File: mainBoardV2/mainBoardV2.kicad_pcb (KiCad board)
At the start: 2 copper layers, 42.8 x 40.5 mm, 30 parts, among them J1 USB4125-GF-A_REVA2, U3 MCP73871-2AAI_ML, U4 MPU6050_Module, U5 TPS61023DRLT

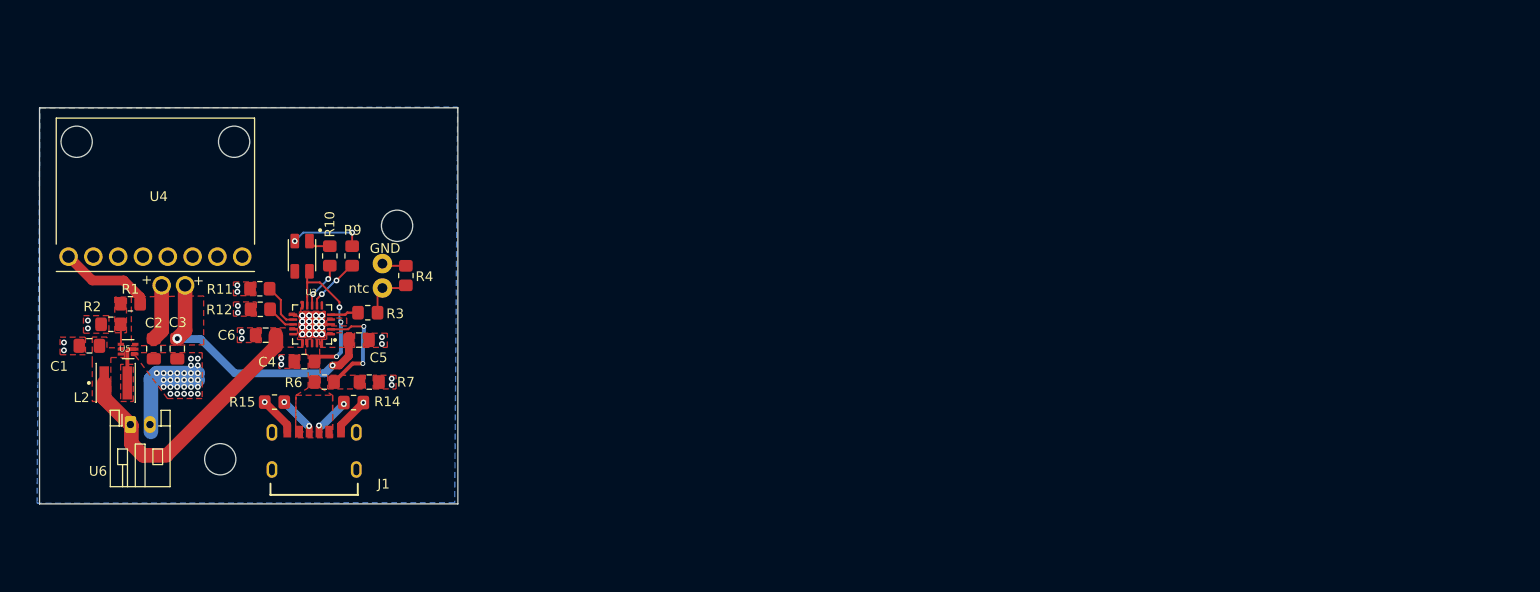
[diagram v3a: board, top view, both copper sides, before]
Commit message: 3.17.26.C2
Added tantalum capacitors to output of boost converter. Have created gerber and drill files after running DRC check until only thing left were some clearance warnings. manufacturer can handle.
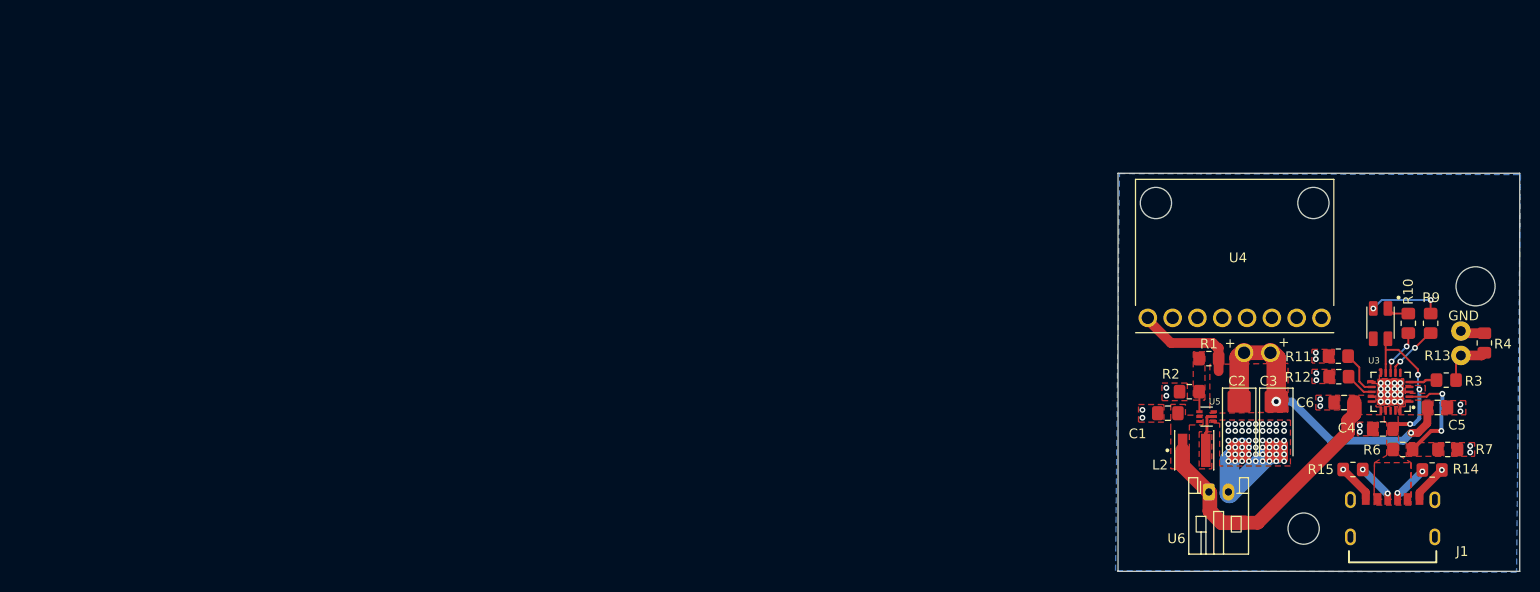
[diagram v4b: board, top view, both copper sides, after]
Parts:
- C2, C3: footprint Capacitor_SMD:C_0805_2012Metric_Pad1.18x1.45mm_HandSolder -> Capacitor_Tantalum_SMD:CP_EIA-6032-15_Kemet-U_HandSolder
- R10: value 470k -> 300
- R9: value 470k -> 160
- moved C3 112.8 mm to (216.8, 125.3)
- moved C2 111.4 mm to (213.0, 125.3)
- moved ? 111.3 mm to (216.2, 117.7)
- moved ? 111.1 mm to (219.6, 135.7)
- moved ? 111.0 mm to (213.5, 117.7)
- moved U4 110.7 mm to (212.5, 107.8)
- moved C5 110.6 mm to (233.3, 123.3)
- moved C6 110.6 mm to (223.8, 122.8)
- moved J1 110.6 mm to (228.7, 135.8)
- moved L2 110.6 mm to (208.4, 127.7)
- moved R10 110.6 mm to (230.3, 114.7)
- moved R11 110.6 mm to (223.2, 118.0)
- moved R14 110.6 mm to (232.8, 129.7)
- moved R15 110.6 mm to (224.7, 129.7)
- moved R2 110.6 mm to (207.9, 121.7)
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- renumbered ntc to R13
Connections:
- U4 pad GND: unconnected-(U4-PadGND) -> GND
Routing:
- net GND: track 26.4 -> 22.8 mm, vias 78 -> 88
- net /VBatt+: track 28.4 -> 30.3 mm
- net /VoutBoost: track 42.7 -> 43.6 mm
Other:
- board size 42.8 x 40.5 mm -> 41.1 x 40.7 mm

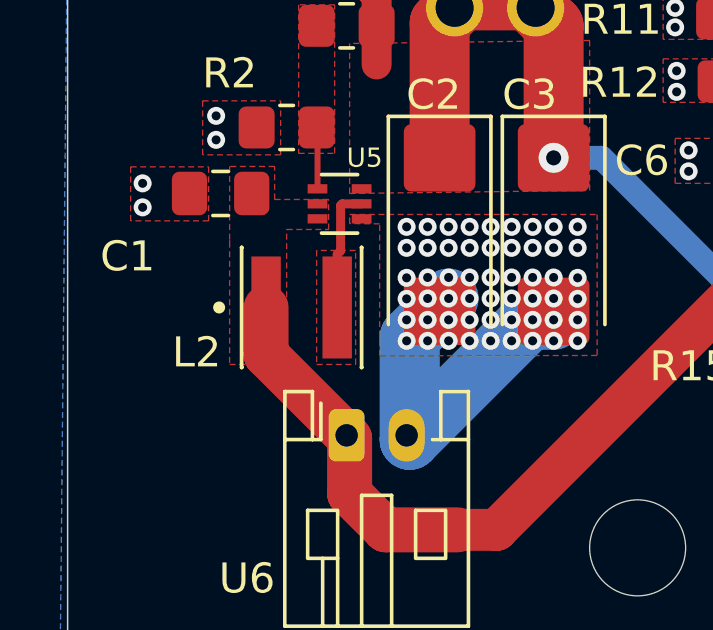
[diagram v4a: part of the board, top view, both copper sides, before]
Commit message: 3.22.26.C1
Added replacement inductor footprint and symbol to library. Updated board and schematic files with new component, but now gerber job files are not coming out correctly. Look transparent in a Gerber Viewer.
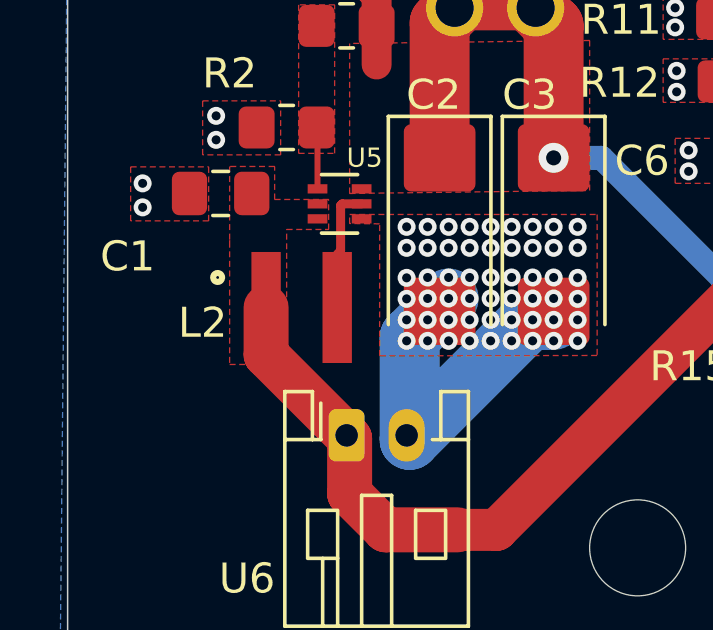
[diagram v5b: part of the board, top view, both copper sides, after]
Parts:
- L2: footprint XEL4030-102MEC:IND_XEL4030-102MEC -> WE-MAPI_4030:WE-MAPI_4030
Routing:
- net /SW: track 4.17 -> 2.40 mm
- removed copper zone on F.Cu, net /SW
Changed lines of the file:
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@@
 		(pcbplotparams
 			(layerselection 0x00000000_00000000_55555555_5755f5ff)
-			(plot_on_all_layers_selection 0x00000000_00000000_00000000_00000000)
+			(plot_on_all_layers_selection 0x00000000_00000000_00000000_0200000c)
 			(disableapertmacros no)
 			(usegerberextensions yes)
@@
 			(drillshape 0)
 			(scaleselection 1)
-			(outputdirectory "fabricationFiles/")
+			(outputdirectory "C:/Users/edwin/Documents/GitHub/mainBoardProject/mainBoardV2/fabricationFiles2/")
 		)
 	)
@@
 		(embedded_fonts no)
 	)
-	(footprint "XEL4030-102MEC:IND_XEL4030-102MEC"
+	(footprint "WE-MAPI_4030:WE-MAPI_4030"
 		(layer "F.Cu")
 		(at 208.4 127.6875)
 		(property "Reference" "L2"
-			(at -3.5 1.5 0)
+			(at -3.3 0.5125 0)
 			(layer "F.SilkS")
 			(effects
@@
 		)
 		(property "Value" "XEL4030-102MEC"
-			(at 8.43 3.135 0)
+			(at 0 3.365 0)
 			(layer "F.Fab")
 			(effects
@@
 		(sheetfile "mainBoardV2.kicad_sch")
 		(attr smd)
-		(fp_line
-			(start -2 -2)
-			(end -1.995 -2)
-			(stroke
-				(width 0.127)
-				(type solid)
-			)
-			(layer "F.SilkS")
-		)
-		(fp_line
-			(start -2 2)
-			(end -2 -2)
-			(stroke
-				(width 0.127)
-				(type solid)
-			)
-			(layer "F.SilkS")
-		)
-		(fp_line
-			(start -1.995 2)
-			(end -2 2)
-			(stroke
-				(width 0.127)
-				(type solid)
-			)
-			(layer "F.SilkS")
-		)
-		(fp_line
-			(start 1.995 -2)
-			(end 2 -2)
-			(stroke
-				(width 0.127)
-				(type solid)
-			)
-			(layer "F.SilkS")
-		)
-		(fp_line
-			(start 2 -2)
-			(end 2 2)
-			(stroke
-				(width 0.127)
-				(type solid)
-			)
-			(layer "F.SilkS")
-		)
-		(fp_line
-			(start 2 2)
-			(end 1.995 2)
-			(stroke
-				(width 0.127)
-				(type solid)
-			)
-			(layer "F.SilkS")
-		)
 		(fp_circle
-			(center -2.75 0)
-			(end -2.65 0)
+			(center -2.8 -1)
+			(end -2.7 -1)
 			(stroke
-				(width 0.2)
+				(width 0.3)
 				(type solid)
 			)
@@
 			(layer "F.SilkS")
 		)
-		(fp_line
-			(start -2.25 -2.25)
-			(end -2.25 2.25)
+		(fp_poly
+			(pts
+				(xy -2.35 -2.35) (xy 2.35 -2.35) (xy 2.35 2.35) (xy -2.35 2.35)
+			)
 			(stroke
-				(width 0.05)
+				(width 0.1)
 				(type solid)
 			)
+			(fill yes)
 			(layer "F.CrtYd")
 		)
 		(fp_line
-			(start -2.25 2.25)
-			(end 2.25 2.25)
+			(start -2.15 -2.15)
+			(end 2.15 -2.15)
 			(stroke
-				(width 0.05)
+				(width 0.2)
 				(type solid)
 			)
-			(layer "F.CrtYd")
+			(layer "F.Fab")
 		)
 		(fp_line
-			(start 2.25 -2.25)
-			(end -2.25 -2.25)
+			(start -2.15 2.15)
+			(end -2.15 -2.15)
 			(stroke
-				(width 0.05)
+				(width 0.2)
 				(type solid)
 			)
-			(layer "F.CrtYd")
+			(layer "F.Fab")
 		)
 		(fp_line
-			(start 2.25 2.25)
-			(end 2.25 -2.25)
+			(start -2.05 -2.05)
+			(end 2.05 -2.05)
 			(stroke
-				(width 0.05)
+				(width 0.1)
 				(type solid)
 			)
-			(layer "F.CrtYd")
+			(layer "F.Fab")
 		)
 		(fp_line
-			(start -2 -2)
-			(end 2 -2)
+			(start -2.05 2.05)
+			(end -2.05 -2.05)
 			(stroke
-				(width 0.127)
+				(width 0.1)
 				(type solid)
 			)
@@
 		)
 		(fp_line
-			(start -2 2)
-			(end -2 -2)
+			(start 2.05 -2.05)
+			(end 2.05 2.05)
 			(stroke
-				(width 0.127)
+				(width 0.1)
 				(type solid)
 			)
@@
 		)
 		(fp_line
-			(start 2 -2)
-			(end 2 2)
+			(start 2.05 2.05)
+			(end -2.05 2.05)
 			(stroke
-				(width 0.127)
+				(width 0.1)
 				(type solid)
 			)
@@
 		)
 		(fp_line
-			(start 2 2)
-			(end -2 2)
+			(start 2.15 -2.15)
+			(end 2.15 2.15)
 			(stroke
-				(width 0.127)
+				(width 0.2)
 				(type solid)
 			)
 			(layer "F.Fab")
 		)
-		(fp_circle
-			(center -2.75 0)
-			(end -2.65 0)
+		(fp_line
+			(start 2.15 2.15)
+			(end -2.15 2.15)
 			(stroke
 				(width 0.2)
 				(type solid)
 			)
-			(fill no)
 			(layer "F.Fab")
 		)
 		(pad "1" smd rect
 			(at -1.185 0)
-			(size 0.98 3.4)
+			(size 0.98 3.7)
 			(layers "F.Cu" "F.Mask" "F.Paste")
 			(net 13 "/VBatt+")
@@
 		(pad "2" smd rect
 			(at 1.185 0)
-			(size 0.98 3.4)
+			(size 0.98 3.7)
 			(layers "F.Cu" "F.Mask" "F.Paste")
 			(net 6 "/SW")
@@
 	)
 	(segment
-		(start 209.585 125.915)
-		(end 209.585 127.6875)
-		(width 0.3)
-		(layer "F.Cu")
-		(net 6)
-	)
-	(segment
 		(start 210.4 124.2335)
 		(end 209.754 124.2335)
@@
 			)
 		)
-	)
-	(zone
-		(net 6)
-		(net_name "/SW")
-		(layer "F.Cu")
-		(hatch edge 0.5)
-		(connect_pads
-			(clearance 0)
-		)
-		(min_thickness 0.25)
-		(filled_areas_thickness no)
-		(fill yes
-			(thermal_gap 0.5)
-			(thermal_bridge_width 0.5)
-		)
-		(polygon
-			(pts
-				(xy 208.9 125.7875) (xy 208.9 129.5875) (xy 210.2 129.5875) (xy 210.2 125.7875)
-			)
-		)

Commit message: Revert "3.22.26.C1"
This reverts commit 781c2ef683714b83309e94a3ccc7edb13d8085a7.
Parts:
- L2: footprint WE-MAPI_4030:WE-MAPI_4030 -> XEL4030-102MEC:IND_XEL4030-102MEC
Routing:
- net /SW: track 2.40 -> 4.17 mm
- added copper zone on F.Cu, net /SW
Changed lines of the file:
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@@
 		(pcbplotparams
 			(layerselection 0x00000000_00000000_55555555_5755f5ff)
-			(plot_on_all_layers_selection 0x00000000_00000000_00000000_0200000c)
+			(plot_on_all_layers_selection 0x00000000_00000000_00000000_00000000)
 			(disableapertmacros no)
 			(usegerberextensions yes)
@@
 			(drillshape 0)
 			(scaleselection 1)
-			(outputdirectory "C:/Users/edwin/Documents/GitHub/mainBoardProject/mainBoardV2/fabricationFiles2/")
+			(outputdirectory "fabricationFiles/")
 		)
 	)
@@
 		(embedded_fonts no)
 	)
-	(footprint "WE-MAPI_4030:WE-MAPI_4030"
+	(footprint "XEL4030-102MEC:IND_XEL4030-102MEC"
 		(layer "F.Cu")
 		(at 208.4 127.6875)
 		(property "Reference" "L2"
-			(at -3.3 0.5125 0)
+			(at -3.5 1.5 0)
 			(layer "F.SilkS")
 			(effects
@@
 		)
 		(property "Value" "XEL4030-102MEC"
-			(at 0 3.365 0)
+			(at 8.43 3.135 0)
 			(layer "F.Fab")
 			(effects
@@
 		(sheetfile "mainBoardV2.kicad_sch")
 		(attr smd)
+		(fp_line
+			(start -2 -2)
+			(end -1.995 -2)
+			(stroke
+				(width 0.127)
+				(type solid)
+			)
+			(layer "F.SilkS")
+		)
+		(fp_line
+			(start -2 2)
+			(end -2 -2)
+			(stroke
+				(width 0.127)
+				(type solid)
+			)
+			(layer "F.SilkS")
+		)
+		(fp_line
+			(start -1.995 2)
+			(end -2 2)
+			(stroke
+				(width 0.127)
+				(type solid)
+			)
+			(layer "F.SilkS")
+		)
+		(fp_line
+			(start 1.995 -2)
+			(end 2 -2)
+			(stroke
+				(width 0.127)
+				(type solid)
+			)
+			(layer "F.SilkS")
+		)
+		(fp_line
+			(start 2 -2)
+			(end 2 2)
+			(stroke
+				(width 0.127)
+				(type solid)
+			)
+			(layer "F.SilkS")
+		)
+		(fp_line
+			(start 2 2)
+			(end 1.995 2)
+			(stroke
+				(width 0.127)
+				(type solid)
+			)
+			(layer "F.SilkS")
+		)
 		(fp_circle
-			(center -2.8 -1)
-			(end -2.7 -1)
+			(center -2.75 0)
+			(end -2.65 0)
 			(stroke
-				(width 0.3)
+				(width 0.2)
 				(type solid)
 			)
@@
 			(layer "F.SilkS")
 		)
-		(fp_poly
-			(pts
-				(xy -2.35 -2.35) (xy 2.35 -2.35) (xy 2.35 2.35) (xy -2.35 2.35)
-			)
+		(fp_line
+			(start -2.25 -2.25)
+			(end -2.25 2.25)
 			(stroke
-				(width 0.1)
+				(width 0.05)
 				(type solid)
 			)
-			(fill yes)
 			(layer "F.CrtYd")
 		)
 		(fp_line
-			(start -2.15 -2.15)
-			(end 2.15 -2.15)
+			(start -2.25 2.25)
+			(end 2.25 2.25)
 			(stroke
-				(width 0.2)
+				(width 0.05)
 				(type solid)
 			)
-			(layer "F.Fab")
+			(layer "F.CrtYd")
 		)
 		(fp_line
-			(start -2.15 2.15)
-			(end -2.15 -2.15)
+			(start 2.25 -2.25)
+			(end -2.25 -2.25)
 			(stroke
-				(width 0.2)
+				(width 0.05)
 				(type solid)
 			)
-			(layer "F.Fab")
+			(layer "F.CrtYd")
 		)
 		(fp_line
-			(start -2.05 -2.05)
-			(end 2.05 -2.05)
+			(start 2.25 2.25)
+			(end 2.25 -2.25)
 			(stroke
-				(width 0.1)
+				(width 0.05)
 				(type solid)
 			)
-			(layer "F.Fab")
+			(layer "F.CrtYd")
 		)
 		(fp_line
-			(start -2.05 2.05)
-			(end -2.05 -2.05)
+			(start -2 -2)
+			(end 2 -2)
 			(stroke
-				(width 0.1)
+				(width 0.127)
 				(type solid)
 			)
@@
 		)
 		(fp_line
-			(start 2.05 -2.05)
-			(end 2.05 2.05)
+			(start -2 2)
+			(end -2 -2)
 			(stroke
-				(width 0.1)
+				(width 0.127)
 				(type solid)
 			)
@@
 		)
 		(fp_line
-			(start 2.05 2.05)
-			(end -2.05 2.05)
+			(start 2 -2)
+			(end 2 2)
 			(stroke
-				(width 0.1)
+				(width 0.127)
 				(type solid)
 			)
@@
 		)
 		(fp_line
-			(start 2.15 -2.15)
-			(end 2.15 2.15)
+			(start 2 2)
+			(end -2 2)
 			(stroke
-				(width 0.2)
+				(width 0.127)
 				(type solid)
 			)
 			(layer "F.Fab")
 		)
-		(fp_line
-			(start 2.15 2.15)
-			(end -2.15 2.15)
+		(fp_circle
+			(center -2.75 0)
+			(end -2.65 0)
 			(stroke
 				(width 0.2)
 				(type solid)
 			)
+			(fill no)
 			(layer "F.Fab")
 		)
 		(pad "1" smd rect
 			(at -1.185 0)
-			(size 0.98 3.7)
+			(size 0.98 3.4)
 			(layers "F.Cu" "F.Mask" "F.Paste")
 			(net 13 "/VBatt+")
@@
 		(pad "2" smd rect
 			(at 1.185 0)
-			(size 0.98 3.7)
+			(size 0.98 3.4)
 			(layers "F.Cu" "F.Mask" "F.Paste")
 			(net 6 "/SW")
@@
 	)
 	(segment
+		(start 209.585 125.915)
+		(end 209.585 127.6875)
+		(width 0.3)
+		(layer "F.Cu")
+		(net 6)
+	)
+	(segment
 		(start 210.4 124.2335)
 		(end 209.754 124.2335)
@@
 			)
 		)
+	)
+	(zone
+		(net 6)
+		(net_name "/SW")
+		(layer "F.Cu")
+		(hatch edge 0.5)
+		(connect_pads
+			(clearance 0)
+		)
+		(min_thickness 0.25)
+		(filled_areas_thickness no)
+		(fill yes
+			(thermal_gap 0.5)
+			(thermal_bridge_width 0.5)
+		)
+		(polygon
+			(pts
+				(xy 208.9 125.7875) (xy 208.9 129.5875) (xy 210.2 129.5875) (xy 210.2 125.7875)
+			)
+		)
